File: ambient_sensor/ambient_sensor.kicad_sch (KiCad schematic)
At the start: 19 parts, among them J1 Conn_01x02_Pin, J2 Conn_01x05_Pin, J3 Conn_01x03_Pin, J4 Conn_01x06_Pin, J5 Conn_01x04_Pin, J6 Micro_SD_Card, U4 ATmega328-P, U6 LD1117S33TR_SOT223, Y1 Crystal

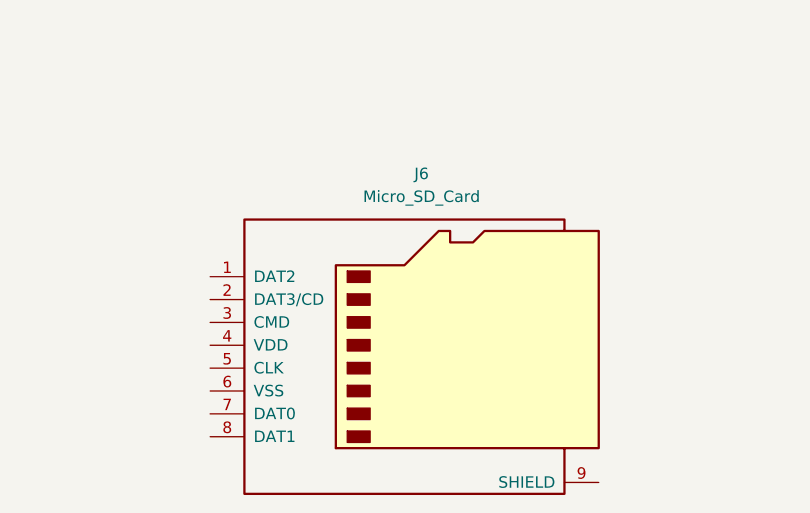
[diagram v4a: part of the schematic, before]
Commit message: microSD reader
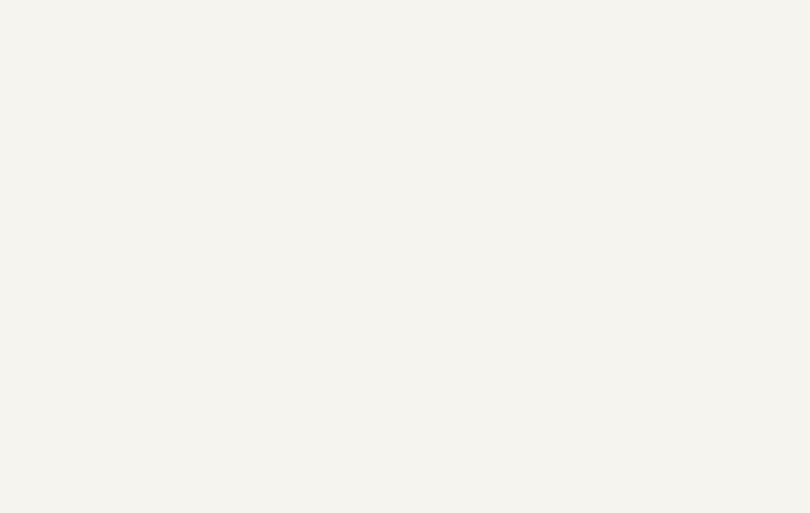
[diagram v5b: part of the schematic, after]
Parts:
- removed J6: Micro_SD_Card, symbol Connector:Micro_SD_Card
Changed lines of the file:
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@@
-	)
-	(symbol
-		(lib_id "Connector:Micro_SD_Card")
-		(at 106.68 147.32 0)
-		(unit 1)
-		(exclude_from_sim no)
-		(in_bom yes)
-		(on_board yes)
-		(dnp no)
-		(fields_autoplaced yes)
-		(property "Reference" "J6"
-			(at 107.315 128.27 0)
-			(effects
-				(font
-					(size 1.27 1.27)
-				)
-			)
-		)
-		(property "Value" "Micro_SD_Card"
-			(at 107.315 130.81 0)
-			(effects
-				(font
-					(size 1.27 1.27)
-				)
-			)
-		)
-		(property "Footprint" ""
-			(at 135.89 139.7 0)
-			(effects
-				(font
-					(size 1.27 1.27)
-				)
-				(hide yes)
-			)
-		)
-		(property "Datasheet" "https://www.we-online.com/components/products/datasheet/693072010801.pdf"
-			(at 106.68 147.32 0)
-			(effects
-				(font
-					(size 1.27 1.27)
-				)
-				(hide yes)
-			)
-		)
-		(property "Description" "Micro SD Card Socket"
-			(at 106.68 147.32 0)
-			(effects
-				(font
-					(size 1.27 1.27)
-				)
-				(hide yes)
-			)
-		)
-		(pin "8"
-		)
-		(pin "9"
-		)
-		(pin "7"
-		)
-		(pin "2"
-		)
-		(pin "4"
-		)
-		(pin "5"
-		)
-		(pin "1"
-		)
-		(pin "6"
-		)
-		(pin "3"
-		)
-		(instances
-			(project ""
-				(path "/9e64b25d-56eb-4d28-941d-8d1b0cd0a88c"
-					(reference "J6")
-					(unit 1)
-				)
-			)
-		)
 	)
 	(symbol

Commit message: microSD reader connected
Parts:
- removed J3: Conn_01x03_Pin, Connector_PinHeader_2.54mm:PinHeader_1x03_P2.54mm_Vertical, symbol Connector:Conn_01x03_Pin
- added R3: 10k, Resistor_SMD:R_1206_3216Metric, symbol Device:R
- added U5: ~, sensors:AdaMicroSD, symbol sensors:AdaMicroSD
- U2: footprint sensors:Si7021original -> sensors:Si7021Original
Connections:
- net +4V: now also R3.1, U5.1 (5V)
- net GND: now also U5.3 (GND)
- net CS: now reaches C2.1, U4.10 (XTAL2/PB7), Y1.1
- net CS: now also U5.7 (CS)
- net DI: now reaches U4.11 (PD5)
- net DI: now also U5.6 (DI)
- net DO: now reaches U4.12 (PD6)
- net DO: now also U5.5 (DO)
- net CLK: now reaches U4.13 (PD7)
- net CLK: now also U5.4 (CLK)
- new net CD: R3.2, U5.8 (CD)
- no-connect marks 25 -> 5

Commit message: sketch for the PCB layout
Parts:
- removed J4: Conn_01x06_Pin, Connector_PinHeader_2.54mm:PinHeader_1x06_P2.54mm_Vertical, symbol Connector:Conn_01x06_Pin
- added J3: Conn_01x05_Pin, Connector_PinHeader_2.54mm:PinHeader_1x05_P2.54mm_Vertical, symbol Connector:Conn_01x05_Pin
- added J4: Conn_01x01_Pin, Connector_PinHeader_2.54mm:PinHeader_1x01_P2.54mm_Vertical, symbol Connector:Conn_01x01_Pin
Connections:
- net at U4.14 (PB0): now also J4.1 (Pin_1)
- net at U4.15 (PB1): now also J3.1 (Pin_1)
- net at U4.16 (PB2): now also J3.2 (Pin_2)
- net at U4.17 (PB3): now also J3.3 (Pin_3)
- net at U4.18 (PB4): now also J3.4 (Pin_4)
- net at U4.19 (PB5): now also J3.5 (Pin_5)
- net Vin: now reaches BT1.1 (+), U6.3 (VI)
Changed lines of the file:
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@@
+		)
+	)
+	(label "Vin"
+		(at 161.29 97.79 0)
+		(fields_autoplaced yes)
+		(effects
+			(font
+				(size 1.27 1.27)
+			)
+			(justify left bottom)
 		)
 	)
@@
 	)
 	(symbol
-		(lib_id "Connector:Conn_01x06_Pin")
-		(at 64.77 34.29 0)
-		(mirror y)
-		(unit 1)
-		(exclude_from_sim no)
-		(in_bom yes)
-		(on_board yes)
-		(dnp no)
-		(fields_autoplaced yes)
-		(property "Reference" "J4"
-			(at 66.04 34.2899 0)
-			(effects
-				(font
-					(size 1.27 1.27)
-				)
-				(justify right)
-			)
-		)
-		(property "Value" "Conn_01x06_Pin"
-			(at 66.04 36.8299 0)
-			(effects
-				(font
-					(size 1.27 1.27)
-				)
-				(justify right)
-			)
-		)
-		(property "Footprint" "Connector_PinHeader_2.54mm:PinHeader_1x06_P2.54mm_Vertical"
-			(at 64.77 34.29 0)
-			(effects
-				(font
-					(size 1.27 1.27)
-				)
-				(hide yes)
-			)
-		)
-		(property "Datasheet" "~"
-			(at 64.77 34.29 0)
-			(effects
-				(font
-					(size 1.27 1.27)
-				)
-				(hide yes)
-			)
-		)
-		(property "Description" "Generic connector, single row, 01x06, script generated"
-			(at 64.77 34.29 0)
-			(effects
-				(font
-					(size 1.27 1.27)
-				)
-				(hide yes)
-			)
-		)
-		(pin "6"
-		)
-		(pin "2"
-		)
-		(pin "5"
-		)
-		(pin "4"
-		)
-		(pin "3"
-		)
-		(pin "1"
-		)
-		(instances
-			(project ""
-				(path "/9e64b25d-56eb-4d28-941d-8d1b0cd0a88c"
-					(reference "J4")
-					(unit 1)
-				)
-			)
-		)
-	)
-	(symbol
 		(lib_id "Device:C")
 		(at 91.44 41.91 90)
@@
 				(path "/9e64b25d-56eb-4d28-941d-8d1b0cd0a88c"
 					(reference "C1")
+					(unit 1)
+				)
+			)
+		)
+	)
+	(symbol
+		(lib_id "Connector:Conn_01x01_Pin")
+		(at 64.77 29.21 0)
+		(mirror y)
+		(unit 1)
+		(exclude_from_sim no)
+		(in_bom yes)
+		(on_board yes)
+		(dnp no)
+		(property "Reference" "J4"
+			(at 73.152 26.67 0)
+			(effects
+				(font
+					(size 1.27 1.27)
+				)
+			)
+		)
+		(property "Value" "Conn_01x01_Pin"
+			(at 73.152 29.21 0)
+			(effects
+				(font
+					(size 1.27 1.27)
+				)
+			)
+		)
+		(property "Footprint" "Connector_PinHeader_2.54mm:PinHeader_1x01_P2.54mm_Vertical"
+			(at 64.77 29.21 0)
+			(effects
+				(font
+					(size 1.27 1.27)
+				)
+				(hide yes)
+			)
+		)
+		(property "Datasheet" "~"
+			(at 64.77 29.21 0)
+			(effects
+				(font
+					(size 1.27 1.27)
+				)
+				(hide yes)
+			)
+		)
+		(property "Description" "Generic connector, single row, 01x01, script generated"
+			(at 64.77 29.21 0)
+			(effects
+				(font
+					(size 1.27 1.27)
+				)
+				(hide yes)
+			)
+		)
+		(pin "1"
+		)
+		(instances
+			(project ""
+				(path "/9e64b25d-56eb-4d28-941d-8d1b0cd0a88c"
+					(reference "J4")
 					(unit 1)
 				)
@@
 					(unit 1)
 				)
+			)
+		)
+	)
+	(symbol
+		(lib_id "Connector:Conn_01x05_Pin")
+		(at 64.77 36.83 0)
+		(mirror y)
+		(unit 1)
+		(exclude_from_sim no)
+		(in_bom yes)
+		(on_board yes)
+		(dnp no)
+		(fields_autoplaced yes)
+		(property "Reference" "J3"
+			(at 66.04 35.5599 0)
+			(effects
+				(font
+					(size 1.27 1.27)
+				)
+				(justify right)
+			)
+		)
+		(property "Value" "Conn_01x05_Pin"
+			(at 66.04 38.0999 0)
+			(effects
+				(font
+					(size 1.27 1.27)
+				)
+				(justify right)
+			)
+		)
+		(property "Footprint" "Connector_PinHeader_2.54mm:PinHeader_1x05_P2.54mm_Vertical"
+			(at 64.77 36.83 0)
+			(effects
+				(font
+					(size 1.27 1.27)
+				)
+				(hide yes)
+			)
+		)
+		(property "Datasheet" "~"
+			(at 64.77 36.83 0)
+			(effects
+				(font
+					(size 1.27 1.27)
+				)
+				(hide yes)
+			)
+		)
+		(property "Description" "Generic connector, single row, 01x05, script generated"
+			(at 64.77 36.83 0)
+			(effects
+				(font
+					(size 1.27 1.27)
+				)
+				(hide yes)
+			)
+		)
+		(pin "4"
+		)
+		(pin "3"
+		)
+		(pin "2"
+		)
+		(pin "1"
+		)
+		(pin "5"
+		)
+		(instances
+			(project ""
+				(path "/9e64b25d-56eb-4d28-941d-8d1b0cd0a88c"
+					(reference "J3")
+					(unit 1)
+				)

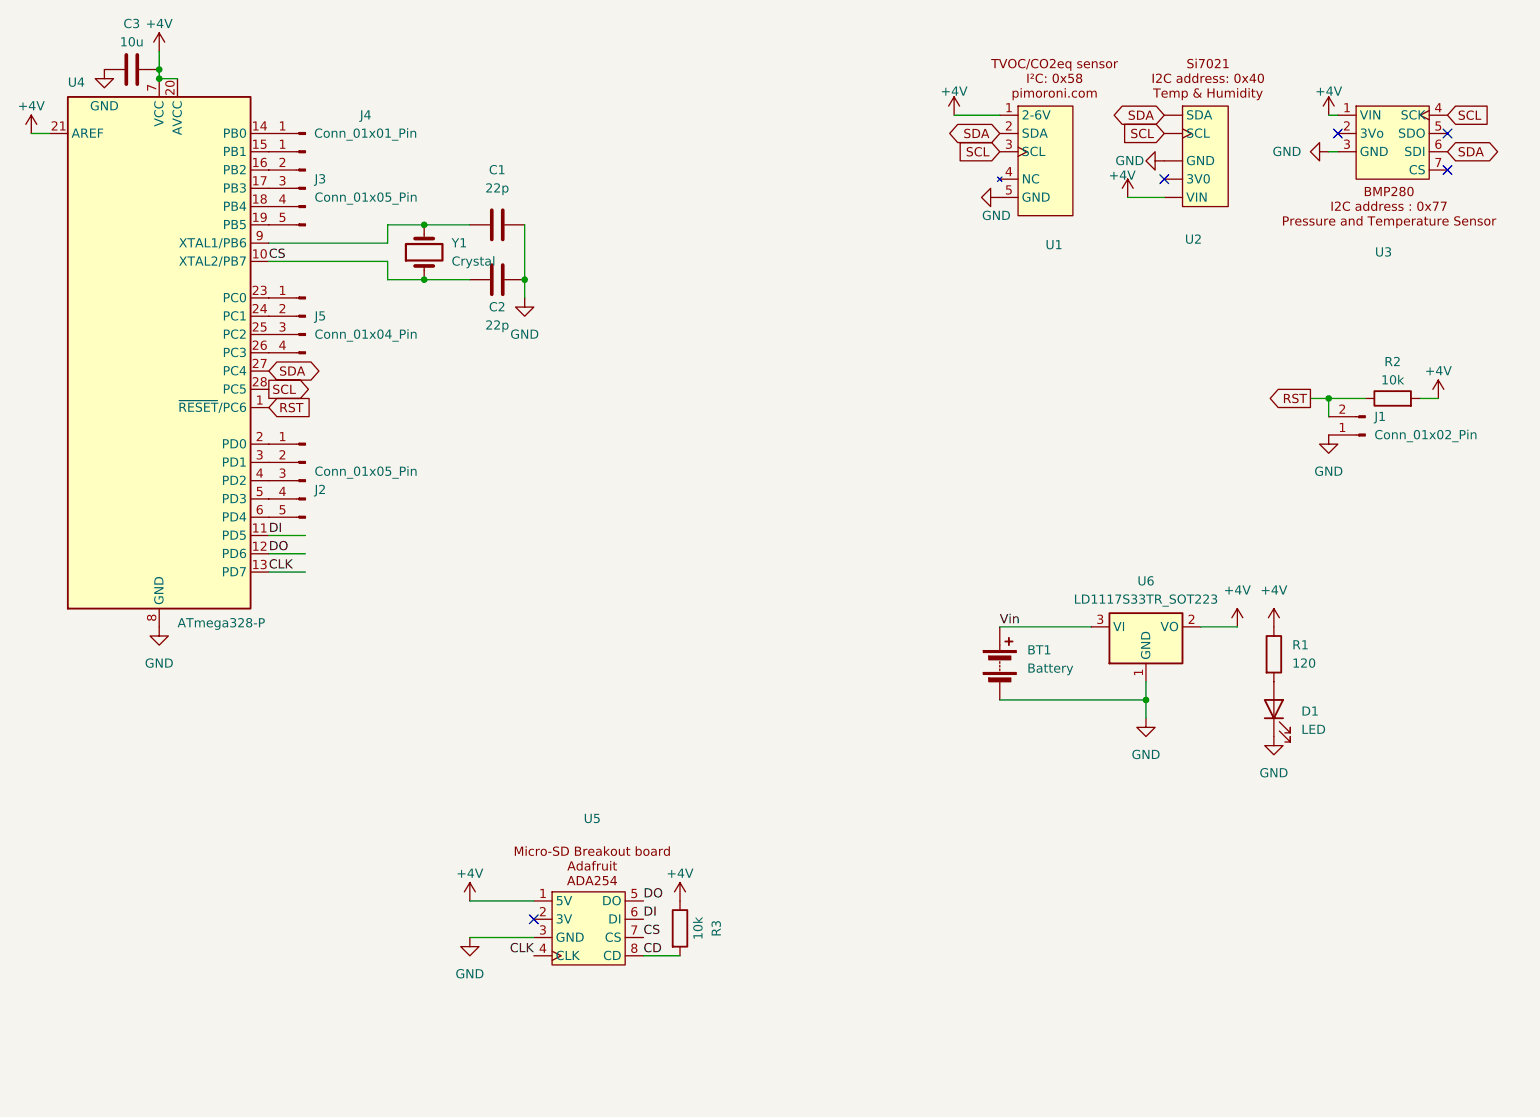
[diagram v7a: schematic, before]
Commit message: add SD card reader, delete micro SD reader, fix Si7072 bugged symbol
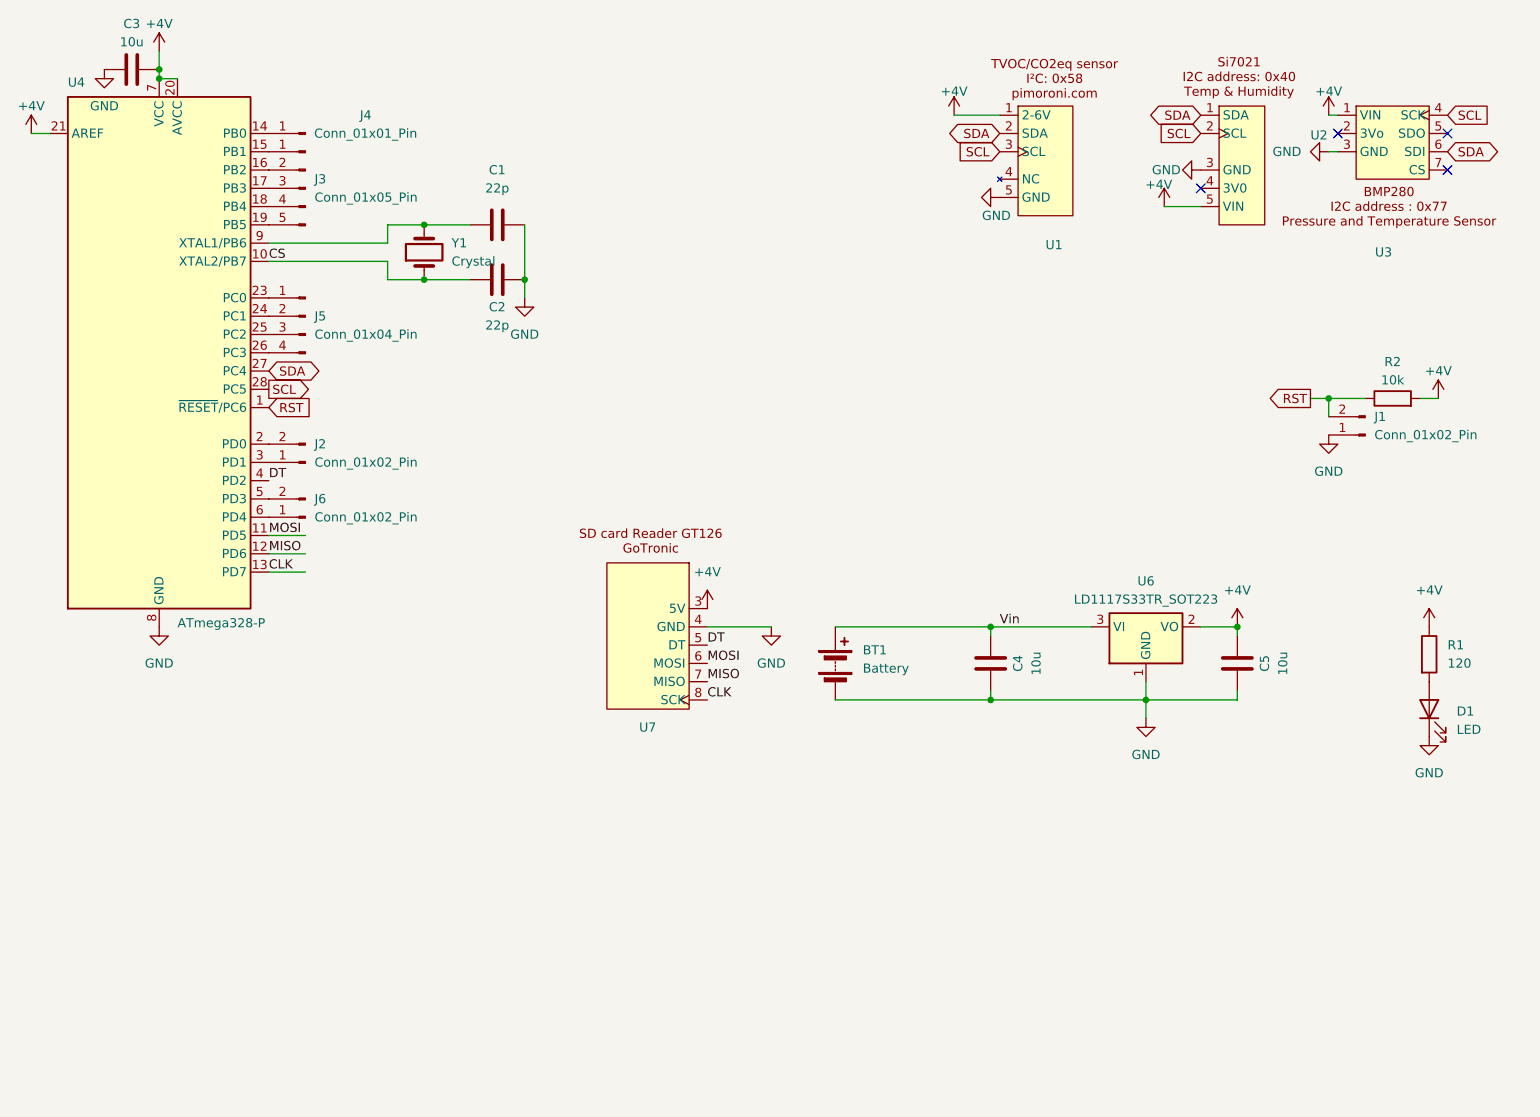
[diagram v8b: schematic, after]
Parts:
- removed J2: Conn_01x05_Pin, Connector_PinHeader_2.54mm:PinHeader_1x05_P2.54mm_Vertical, symbol Connector:Conn_01x05_Pin
- removed R3: 10k, Resistor_SMD:R_1206_3216Metric, symbol Device:R
- removed U2: ~, sensors:Si7021Original, symbol sensors:Si7021Original
- removed U5: ~, sensors:AdaMicroSD, symbol sensors:AdaMicroSD
- added C4, C5: 10u, Capacitor_SMD:C_1206_3216Metric, symbol Device:C
- added J2, J6: Conn_01x02_Pin, Connector_PinHeader_2.54mm:PinHeader_1x02_P2.54mm_Vertical, symbol Connector:Conn_01x02_Pin
- added U2: ~, sensors:Si7021_original, symbol sensors:Si7021
- added U7: ~, sensors:SD_reader_goTronic, symbol sensors:SD_reader_gotronic
- BT1: footprint (none) -> Connector_PinHeader_2.54mm:PinHeader_1x02_P2.54mm_Vertical
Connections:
- net +4V: now also C5.2, U2.5 (VIN), U7.3 (5V)
- net CLK: now also U7.8 (SCK)
- net GND: now also C4.1, C5.1, U2.3 (GND), U7.4 (GND)
- net SCL: now also U2.2 (SCL)
- net SDA: now also U2.1 (SDA)
- net Vin: now also C4.2
- net at U4.2 (PD0): now also J2.2 (Pin_2)
- net at U4.3 (PD1): now also J2.1 (Pin_1)
- net DT: now reaches U4.4 (PD2)
- net DT: now also U7.5 (DT)
- net at U4.5 (PD3): now also J6.2 (Pin_2)
- net at U4.6 (PD4): now also J6.1 (Pin_1)
- net DI renamed MOSI
- net MOSI: now also U7.6 (MOSI)
- net DO renamed MISO
- net MISO: now also U7.7 (MISO)
- no-connect marks 5 -> 4
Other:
- moved on the sheet: BT1, D1, R1
